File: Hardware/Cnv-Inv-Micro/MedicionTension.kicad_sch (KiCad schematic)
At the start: 10 parts, among them U17 TL431PK, U18 PC817

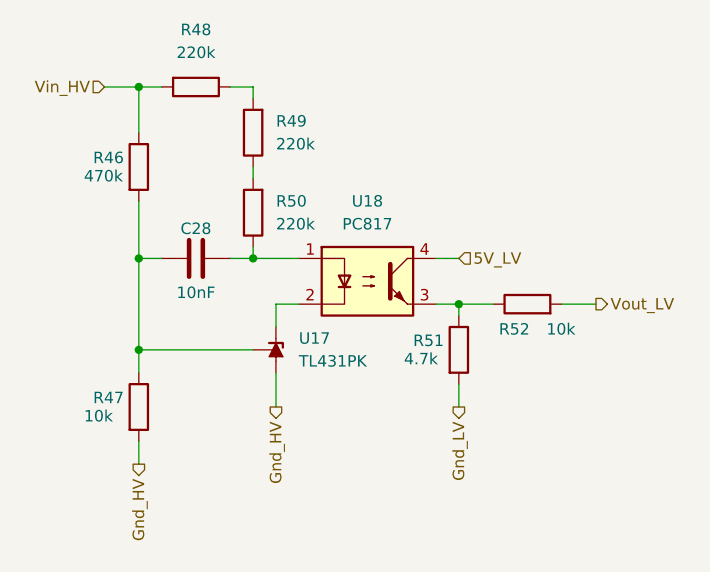
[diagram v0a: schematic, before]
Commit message: Avances en PCB conversor y inversor - Simulaciones de modulacion
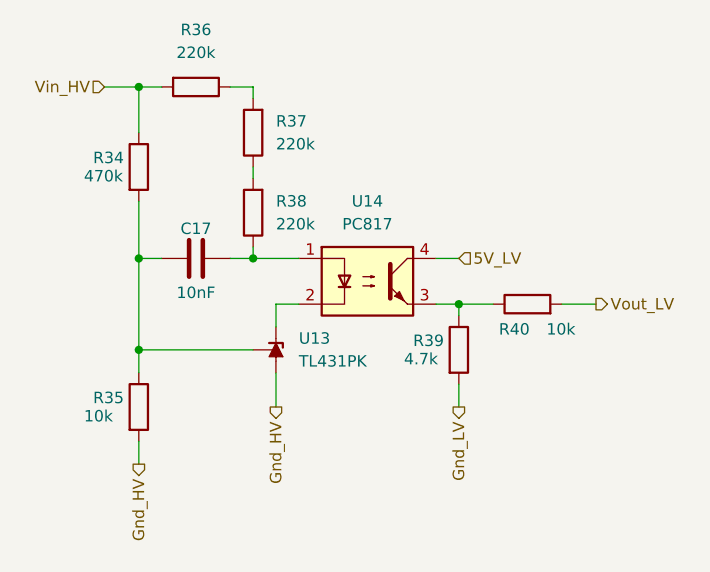
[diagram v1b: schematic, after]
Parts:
- renumbered C28 to C17, R46 to R34, R47 to R35, R48 to R36, R49 to R37, R50 to R38, R51 to R39, R52 to R40, U17 to U13, U18 to U14
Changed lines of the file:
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@@
 		(dnp no)
 		(fields_autoplaced yes)
-		(property "Reference" "U18"
+		(property "Reference" "U14"
 			(at 142.24 93.98 0)
 			(effects
@@
 			(project ""
 				(path "/e60c11d9-ab9e-4760-a4a7-008fcec65a72/c6551446-5e26-4d9a-a5bc-1c867d865e21/0a448165-ee74-4b91-8dde-4d35bebf2843"
-					(reference "U18")
-					(unit 1)
-				)
-				(path "/e60c11d9-ab9e-4760-a4a7-008fcec65a72/c6551446-5e26-4d9a-a5bc-1c867d865e21/6ade7ab7-6233-4c60-8ab6-50f492d9a784"
-					(reference "U21")
+					(reference "U14")
+					(unit 1)
+				)
+				(path "/e60c11d9-ab9e-4760-a4a7-008fcec65a72/c6551446-5e26-4d9a-a5bc-1c867d865e21/6ade7ab7-6233-4c60-8ab6-50f492d9a784"
+					(reference "U16")
 					(unit 1)
 				)
@@
 		(on_board yes)
 		(dnp no)
-		(property "Reference" "C28"
+		(property "Reference" "C17"
 			(at 123.19 97.028 90)
 			(effects
@@
 			(project "VFD_V1"
 				(path "/e60c11d9-ab9e-4760-a4a7-008fcec65a72/c6551446-5e26-4d9a-a5bc-1c867d865e21/0a448165-ee74-4b91-8dde-4d35bebf2843"
-					(reference "C28")
-					(unit 1)
-				)
-				(path "/e60c11d9-ab9e-4760-a4a7-008fcec65a72/c6551446-5e26-4d9a-a5bc-1c867d865e21/6ade7ab7-6233-4c60-8ab6-50f492d9a784"
-					(reference "C29")
+					(reference "C17")
+					(unit 1)
+				)
+				(path "/e60c11d9-ab9e-4760-a4a7-008fcec65a72/c6551446-5e26-4d9a-a5bc-1c867d865e21/6ade7ab7-6233-4c60-8ab6-50f492d9a784"
+					(reference "C18")
 					(unit 1)
 				)
@@
 		(dnp no)
 		(fields_autoplaced yes)
-		(property "Reference" "R48"
+		(property "Reference" "R36"
 			(at 123.19 74.93 90)
 			(effects
@@
 			(project "VFD_V1"
 				(path "/e60c11d9-ab9e-4760-a4a7-008fcec65a72/c6551446-5e26-4d9a-a5bc-1c867d865e21/0a448165-ee74-4b91-8dde-4d35bebf2843"
-					(reference "R48")
-					(unit 1)
-				)
-				(path "/e60c11d9-ab9e-4760-a4a7-008fcec65a72/c6551446-5e26-4d9a-a5bc-1c867d865e21/6ade7ab7-6233-4c60-8ab6-50f492d9a784"
-					(reference "R57")
+					(reference "R36")
+					(unit 1)
+				)
+				(path "/e60c11d9-ab9e-4760-a4a7-008fcec65a72/c6551446-5e26-4d9a-a5bc-1c867d865e21/6ade7ab7-6233-4c60-8ab6-50f492d9a784"
+					(reference "R43")
 					(unit 1)
 				)
@@
 		(dnp no)
 		(fields_autoplaced yes)
-		(property "Reference" "R50"
+		(property "Reference" "R38"
 			(at 132.08 93.9799 0)
 			(effects
@@
 			(project "VFD_V1"
 				(path "/e60c11d9-ab9e-4760-a4a7-008fcec65a72/c6551446-5e26-4d9a-a5bc-1c867d865e21/0a448165-ee74-4b91-8dde-4d35bebf2843"
-					(reference "R50")
-					(unit 1)
-				)
-				(path "/e60c11d9-ab9e-4760-a4a7-008fcec65a72/c6551446-5e26-4d9a-a5bc-1c867d865e21/6ade7ab7-6233-4c60-8ab6-50f492d9a784"
-					(reference "R59")
+					(reference "R38")
+					(unit 1)
+				)
+				(path "/e60c11d9-ab9e-4760-a4a7-008fcec65a72/c6551446-5e26-4d9a-a5bc-1c867d865e21/6ade7ab7-6233-4c60-8ab6-50f492d9a784"
+					(reference "R45")
 					(unit 1)
 				)
@@
 		(on_board yes)
 		(dnp no)
-		(property "Reference" "R52"
+		(property "Reference" "R40"
 			(at 160.274 108.204 90)
 			(effects
@@
 			(project "VFD_V1"
 				(path "/e60c11d9-ab9e-4760-a4a7-008fcec65a72/c6551446-5e26-4d9a-a5bc-1c867d865e21/0a448165-ee74-4b91-8dde-4d35bebf2843"
-					(reference "R52")
-					(unit 1)
-				)
-				(path "/e60c11d9-ab9e-4760-a4a7-008fcec65a72/c6551446-5e26-4d9a-a5bc-1c867d865e21/6ade7ab7-6233-4c60-8ab6-50f492d9a784"
-					(reference "R61")
+					(reference "R40")
+					(unit 1)
+				)
+				(path "/e60c11d9-ab9e-4760-a4a7-008fcec65a72/c6551446-5e26-4d9a-a5bc-1c867d865e21/6ade7ab7-6233-4c60-8ab6-50f492d9a784"
+					(reference "R47")
 					(unit 1)
 				)
@@
 		(on_board yes)
 		(dnp no)
-		(property "Reference" "R46"
+		(property "Reference" "R34"
 			(at 111.76 89.154 0)
 			(effects
@@
 			(project "VFD_V1"
 				(path "/e60c11d9-ab9e-4760-a4a7-008fcec65a72/c6551446-5e26-4d9a-a5bc-1c867d865e21/0a448165-ee74-4b91-8dde-4d35bebf2843"
-					(reference "R46")
-					(unit 1)
-				)
-				(path "/e60c11d9-ab9e-4760-a4a7-008fcec65a72/c6551446-5e26-4d9a-a5bc-1c867d865e21/6ade7ab7-6233-4c60-8ab6-50f492d9a784"
-					(reference "R55")
+					(reference "R34")
+					(unit 1)
+				)
+				(path "/e60c11d9-ab9e-4760-a4a7-008fcec65a72/c6551446-5e26-4d9a-a5bc-1c867d865e21/6ade7ab7-6233-4c60-8ab6-50f492d9a784"
+					(reference "R41")
 					(unit 1)
 				)
@@
 		(on_board yes)
 		(dnp no)
-		(property "Reference" "R51"
+		(property "Reference" "R39"
 			(at 147.32 109.474 0)
 			(effects
@@
 			(project "VFD_V1"
 				(path "/e60c11d9-ab9e-4760-a4a7-008fcec65a72/c6551446-5e26-4d9a-a5bc-1c867d865e21/0a448165-ee74-4b91-8dde-4d35bebf2843"
-					(reference "R51")
-					(unit 1)
-				)
-				(path "/e60c11d9-ab9e-4760-a4a7-008fcec65a72/c6551446-5e26-4d9a-a5bc-1c867d865e21/6ade7ab7-6233-4c60-8ab6-50f492d9a784"
-					(reference "R60")
+					(reference "R39")
+					(unit 1)
+				)
+				(path "/e60c11d9-ab9e-4760-a4a7-008fcec65a72/c6551446-5e26-4d9a-a5bc-1c867d865e21/6ade7ab7-6233-4c60-8ab6-50f492d9a784"
+					(reference "R46")
 					(unit 1)
 				)
@@
 		(on_board yes)
 		(dnp no)
-		(property "Reference" "R47"
+		(property "Reference" "R35"
 			(at 111.76 115.824 0)
 			(effects
@@
 			(project "VFD_V1"
 				(path "/e60c11d9-ab9e-4760-a4a7-008fcec65a72/c6551446-5e26-4d9a-a5bc-1c867d865e21/0a448165-ee74-4b91-8dde-4d35bebf2843"
-					(reference "R47")
-					(unit 1)
-				)
-				(path "/e60c11d9-ab9e-4760-a4a7-008fcec65a72/c6551446-5e26-4d9a-a5bc-1c867d865e21/6ade7ab7-6233-4c60-8ab6-50f492d9a784"
-					(reference "R56")
+					(reference "R35")
+					(unit 1)
+				)
+				(path "/e60c11d9-ab9e-4760-a4a7-008fcec65a72/c6551446-5e26-4d9a-a5bc-1c867d865e21/6ade7ab7-6233-4c60-8ab6-50f492d9a784"
+					(reference "R42")
 					(unit 1)
 				)
@@
 		(dnp no)
 		(fields_autoplaced yes)
-		(property "Reference" "U17"
+		(property "Reference" "U13"
 			(at 134.62 109.2199 90)
 			(effects
@@
 			(project ""
 				(path "/e60c11d9-ab9e-4760-a4a7-008fcec65a72/c6551446-5e26-4d9a-a5bc-1c867d865e21/0a448165-ee74-4b91-8dde-4d35bebf2843"
-					(reference "U17")
-					(unit 1)
-				)
-				(path "/e60c11d9-ab9e-4760-a4a7-008fcec65a72/c6551446-5e26-4d9a-a5bc-1c867d865e21/6ade7ab7-6233-4c60-8ab6-50f492d9a784"
-					(reference "U20")
+					(reference "U13")
+					(unit 1)
+				)
+				(path "/e60c11d9-ab9e-4760-a4a7-008fcec65a72/c6551446-5e26-4d9a-a5bc-1c867d865e21/6ade7ab7-6233-4c60-8ab6-50f492d9a784"
+					(reference "U15")
 					(unit 1)
 				)
@@
 		(dnp no)
 		(fields_autoplaced yes)
-		(property "Reference" "R49"
+		(property "Reference" "R37"
 			(at 132.08 85.0899 0)
 			(effects
@@
 			(project "VFD_V1"
 				(path "/e60c11d9-ab9e-4760-a4a7-008fcec65a72/c6551446-5e26-4d9a-a5bc-1c867d865e21/0a448165-ee74-4b91-8dde-4d35bebf2843"
-					(reference "R49")
-					(unit 1)
-				)
-				(path "/e60c11d9-ab9e-4760-a4a7-008fcec65a72/c6551446-5e26-4d9a-a5bc-1c867d865e21/6ade7ab7-6233-4c60-8ab6-50f492d9a784"
-					(reference "R58")
-					(unit 1)
-				)
+					(reference "R37")
+					(unit 1)
+				)
+				(path "/e60c11d9-ab9e-4760-a4a7-008fcec65a72/c6551446-5e26-4d9a-a5bc-1c867d865e21/6ade7ab7-6233-4c60-8ab6-50f492d9a784"
+					(reference "R44")
+					(unit 1)
+				)
